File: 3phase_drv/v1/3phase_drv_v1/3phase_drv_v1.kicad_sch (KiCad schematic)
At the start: 0 parts

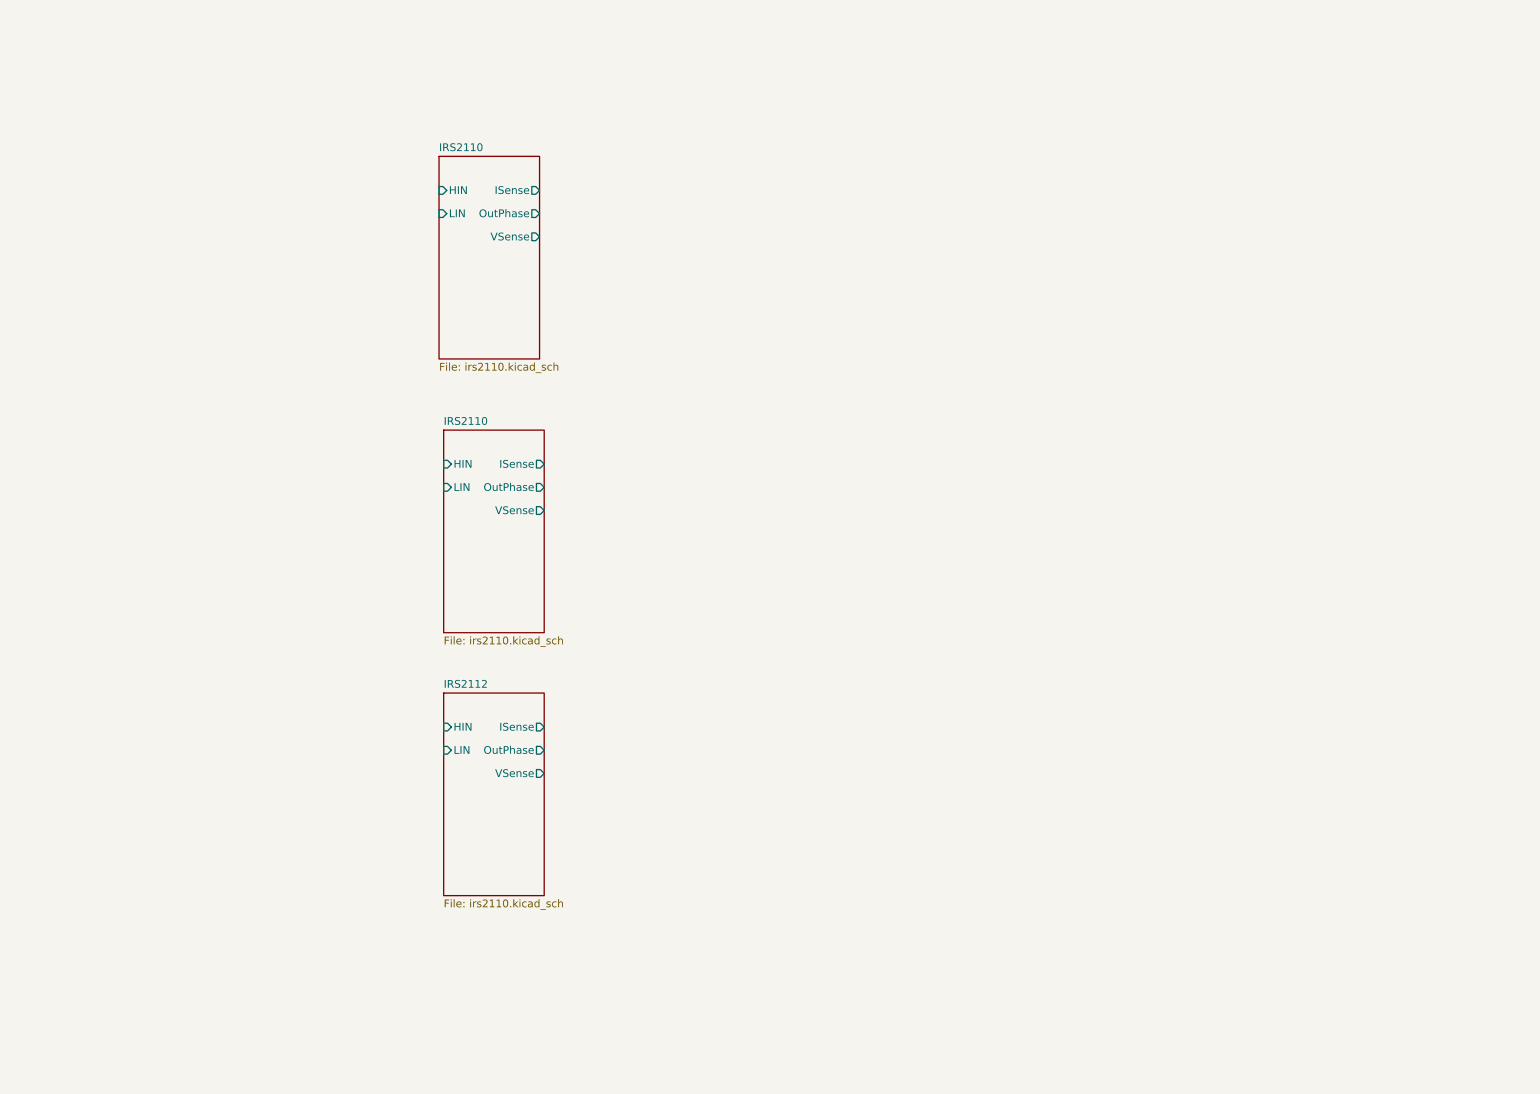
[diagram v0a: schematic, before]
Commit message: update ir2110s schematic and board layout
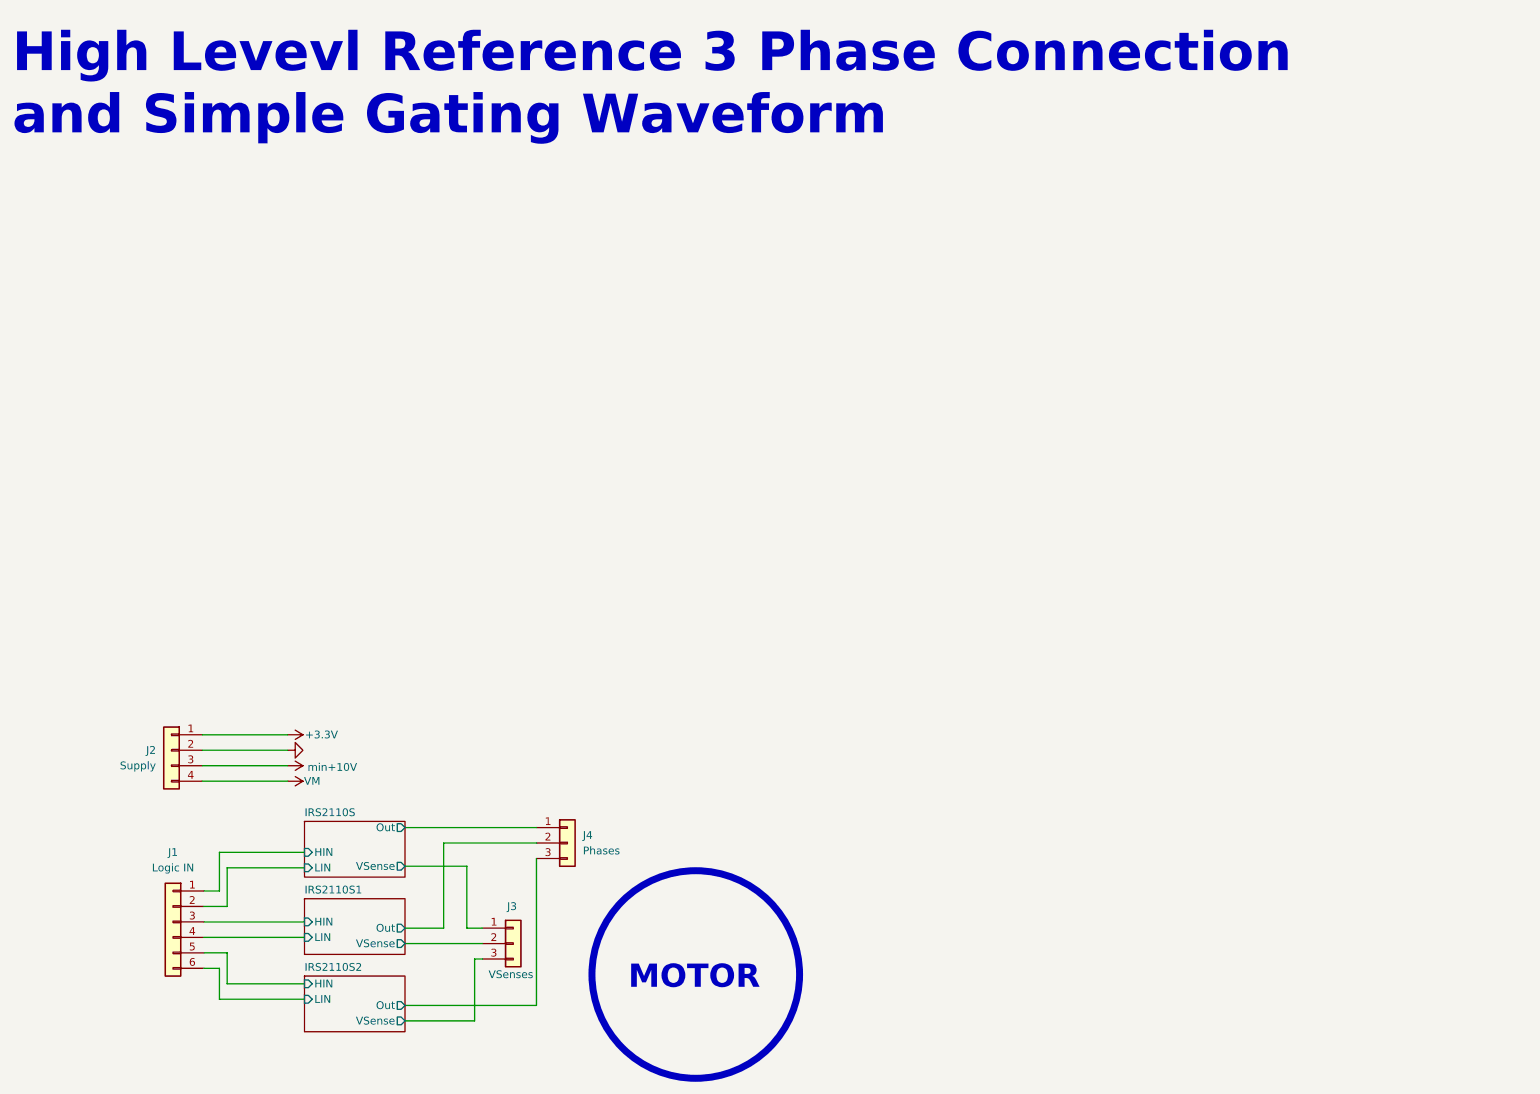
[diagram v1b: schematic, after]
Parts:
- added J1: Logic IN, Connector_PinHeader_2.54mm:PinHeader_1x06_P2.54mm_Vertical, symbol Connector_Generic:Conn_01x06
- added J2: Supply, Connector_PinHeader_2.54mm:PinHeader_1x04_P2.54mm_Vertical, symbol Connector_Generic:Conn_01x04
- added J3: VSenses, Connector_PinHeader_2.54mm:PinHeader_1x03_P2.54mm_Vertical, symbol Connector_Generic:Conn_01x03
- added J4: Phases, Connector_PinHeader_2.54mm:PinHeader_1x03_P2.54mm_Vertical, symbol Connector_Generic:Conn_01x03
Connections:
- new net +3.3V: J2.1 (Pin_1)
- new net GND: J2.2 (Pin_2)
- new net IRS2110S/HIN: J1.1 (Pin_1)
- new net IRS2110S/LIN: J1.2 (Pin_2)
- new net IRS2110S/Out: J4.1 (Pin_1)
- new net IRS2110S/VSense: J3.1 (Pin_1)
- new net IRS2110S1/HIN: J1.3 (Pin_3)
- new net IRS2110S1/LIN: J1.4 (Pin_4)
- new net IRS2110S1/Out: J4.2 (Pin_2)
- new net IRS2110S1/VSense: J3.2 (Pin_2)
- new net IRS2110S2/HIN: J1.5 (Pin_5)
- new net IRS2110S2/LIN: J1.6 (Pin_6)
- new net IRS2110S2/Out: J4.3 (Pin_3)
- new net IRS2110S2/VSense: J3.3 (Pin_3)
- new net VM: J2.4 (Pin_4)
- new net min+10V: J2.3 (Pin_3)
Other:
- removed sheet IRS2110
- removed sheet IRS2112
- added sheet IRS2110S (irs2110.kicad_sch)
- added sheet IRS2110S1 (irs2110.kicad_sch)
- added sheet IRS2110S2 (irs2110.kicad_sch)
- note added: "High Levevl Reference 3 Phase Connection and Simple Gating Waveform"
- note added: "MOTOR"
- title: (none) -> Main Connection And Pinout
